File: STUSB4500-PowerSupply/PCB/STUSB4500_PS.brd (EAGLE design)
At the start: 60 x 40 mm, 90 parts, among them J2 FEMALE 2x3, J3 FEMALE 2x3, J4 FEMALE 2x3

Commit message: UART and 3V3
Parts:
- added F1: 6V/0.5A, DD_SparkFun-Fuses:1206
- added J9: (no value), DD_SparkFun-Connectors:1X03_LOCK_NO_SILK
- moved C17 1.84 mm to (17.8, 27.6), turned to 90 degrees
- moved R39 1.56 mm to (12.0, 34.6)
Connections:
- new net UART_RX: J9.2, U$8.11
- new net UART_TX: J9.1, U$8.12
- net +3V3: now also F1.2
- net GND: now also J9.3
- net VIN_2: now also F1.1
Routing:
- net +3V3: track 149.1 -> 94.3 mm, vias 8 -> 12
- net VIN_2: track 28.2 -> 82.5 mm, vias 0 -> 6
- net UART_RX: track 0.00 -> 7.32 mm
- net UART_TX: track 0.00 -> 6.15 mm
- net N$27: track 4.42 -> 2.86 mm
- net USB_D+: track 22.3 -> 21.2 mm
- net USB_D-: track 23.3 -> 22.2 mm
- net GND: vias 165 -> 167
- added copper zone on layer 16, net VIN_2
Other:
- board text added: "Dyringer"

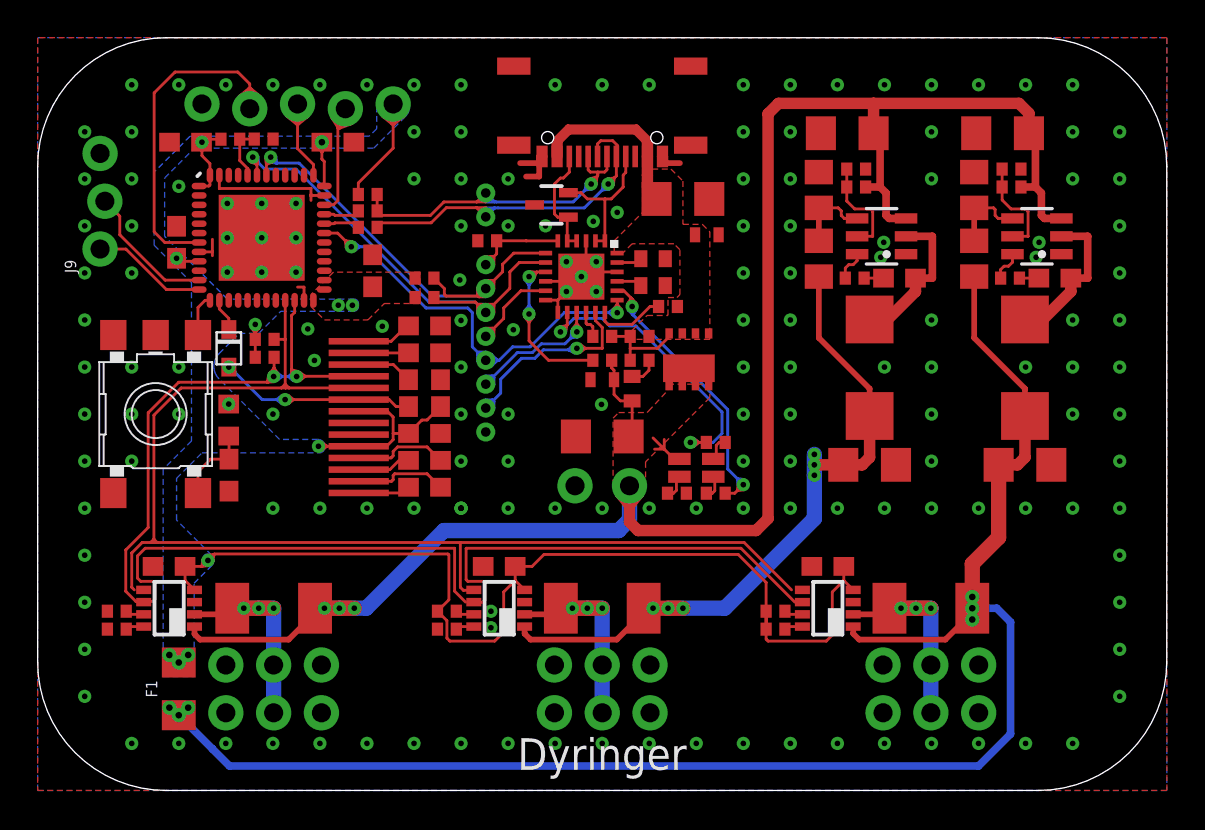
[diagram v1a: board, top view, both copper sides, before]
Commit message: Added output caps and diodes
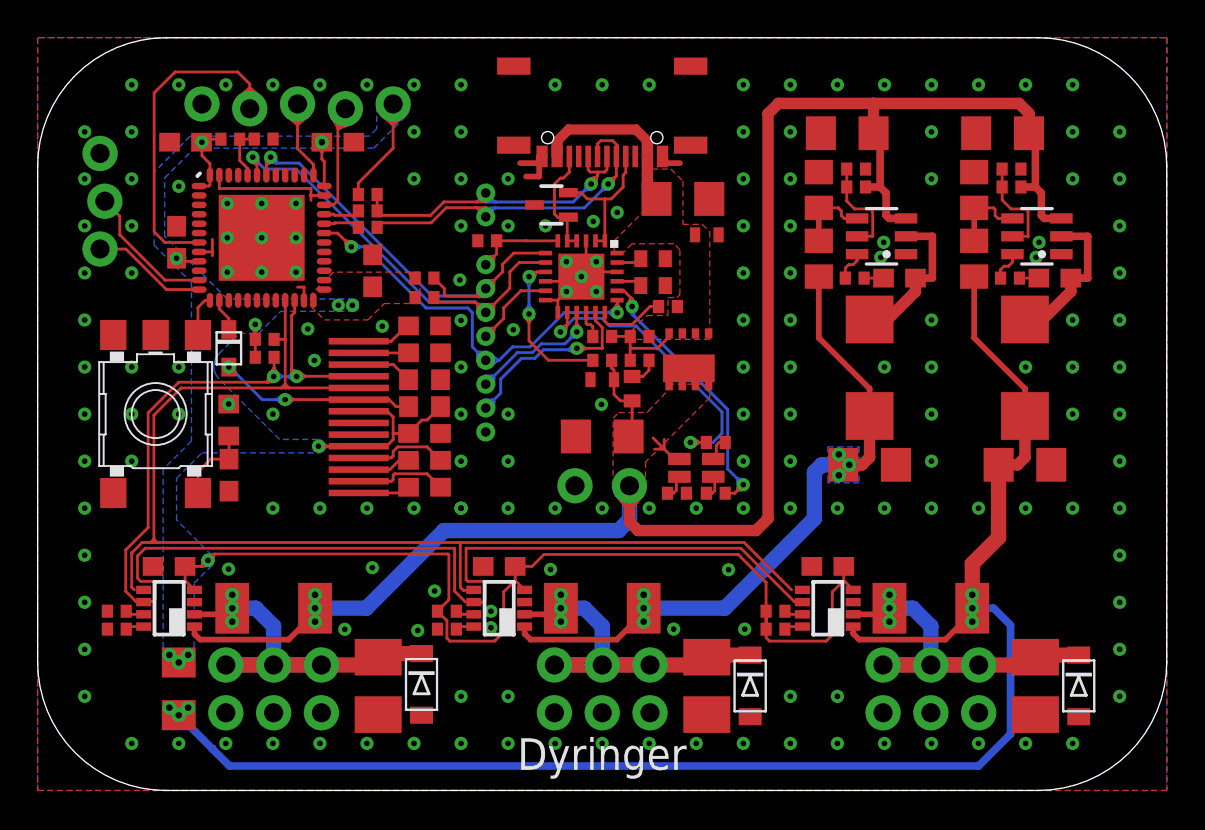
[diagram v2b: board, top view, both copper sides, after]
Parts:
- added C25, C26, C27: (no value), DD_rcl:B/3528-21R
- added D1, D3, D4: (no value), DD_adafruit:SOD-123FL
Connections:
- net VIN_1 renamed 5V0_IN
- removed net VOUT_0: J4.3, J4.4, R19.1, U$10.2
- removed net VOUT_1: J2.3, J2.4, R8.1, U$7.2
- removed net VOUT_2: J3.3, J3.4, R14.1, U$9.2
- new net 3V3_IN: C13.2, L2.2, R14.2, R24.2, U$9.1
- new net 3V3_OUT: C26.+, D3.C, J3.2, J3.4, J3.6, R14.1, U$9.2
- new net 5V0_OUT: C25.+, D4.C, J2.2, J2.4, J2.6, R8.1, U$7.2
- new net USB-PD_OUT: C27.+, D1.C, J4.2, J4.4, J4.6, R19.1, U$10.2
- net GND: now also C25.-, C26.-, C27.-, D1.A, D3.A, D4.A, J2.3, J3.3, J4.3; no longer J2.2, J2.6, J3.2, J3.6, J4.2, J4.6
- net VIN_2: no longer C13.2, L2.2, R14.2, R24.2, U$9.1
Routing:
- net VIN_2: track 82.5 -> 54.2 mm
- net 3V3_IN: track 0.00 -> 27.9 mm
- net USB-PD_OUT: track 0.00 -> 22.9 mm, vias 0 -> 3
- net 5V0_OUT: track 0.00 -> 22.3 mm, vias 0 -> 3
- net 3V3_OUT: track 0.00 -> 22.3 mm, vias 0 -> 3
- net VOUT_0: track 11.5 -> 0.00 mm, vias 3 -> 0
- net VOUT_2: track 11.4 -> 0.00 mm, vias 3 -> 0
- net VOUT_1: track 11.4 -> 0.00 mm, vias 3 -> 0
- net USB_PD_VDD: track 101.3 -> 100.2 mm
- net 5V0_IN: track 36.7 -> 35.7 mm
- net GND: vias 167 -> 180
- added copper zone on layer 16, net 3V3_OUT
- added copper zone on layer 16, net 5V0_IN
- added copper zone on layer 16, net 5V0_OUT
- added copper zone on layer 16, net USB-PD_OUT
- added copper zone on layer 16, net USB_PD_VDD

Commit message: Cleanups replaced button with adafruit one
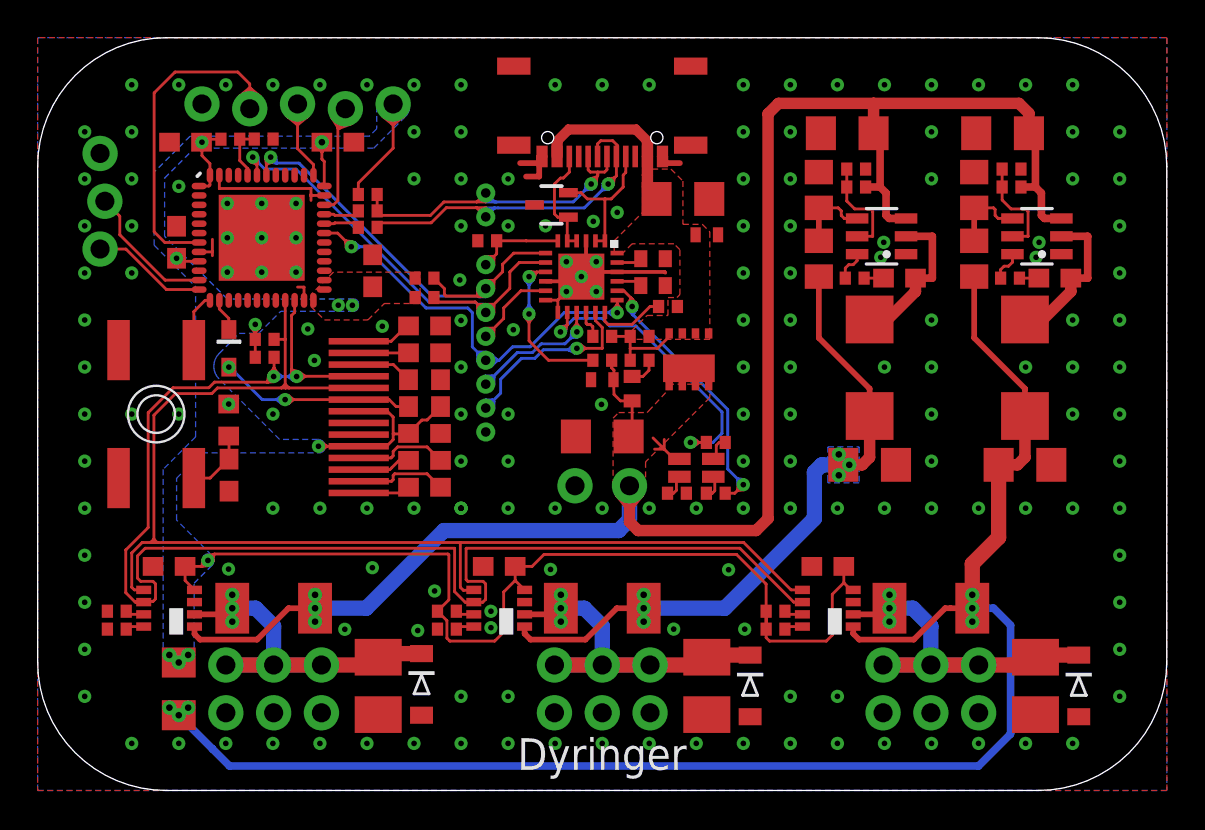
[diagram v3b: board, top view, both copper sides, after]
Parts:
- removed S1: SKHMPSE010, switch:SKHMPXE010
- added SW1: SPST_TACT-EVQQ2, DD_adafruit:EVQ-Q2
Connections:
- net GND: now also SW1.A, SW1.A'; no longer S1.1, S1.2, S1.5
- net KEY: now also SW1.B, SW1.B'; no longer S1.3, S1.4
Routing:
- net GND: track 25.2 -> 33.1 mm, vias 180 -> 177
- net SDA_2: track 82.8 -> 84.3 mm
- net SCL_2: track 66.2 -> 67.4 mm
- net USB_PD_VDD: track 100.2 -> 101.3 mm

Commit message: Updated stusb part
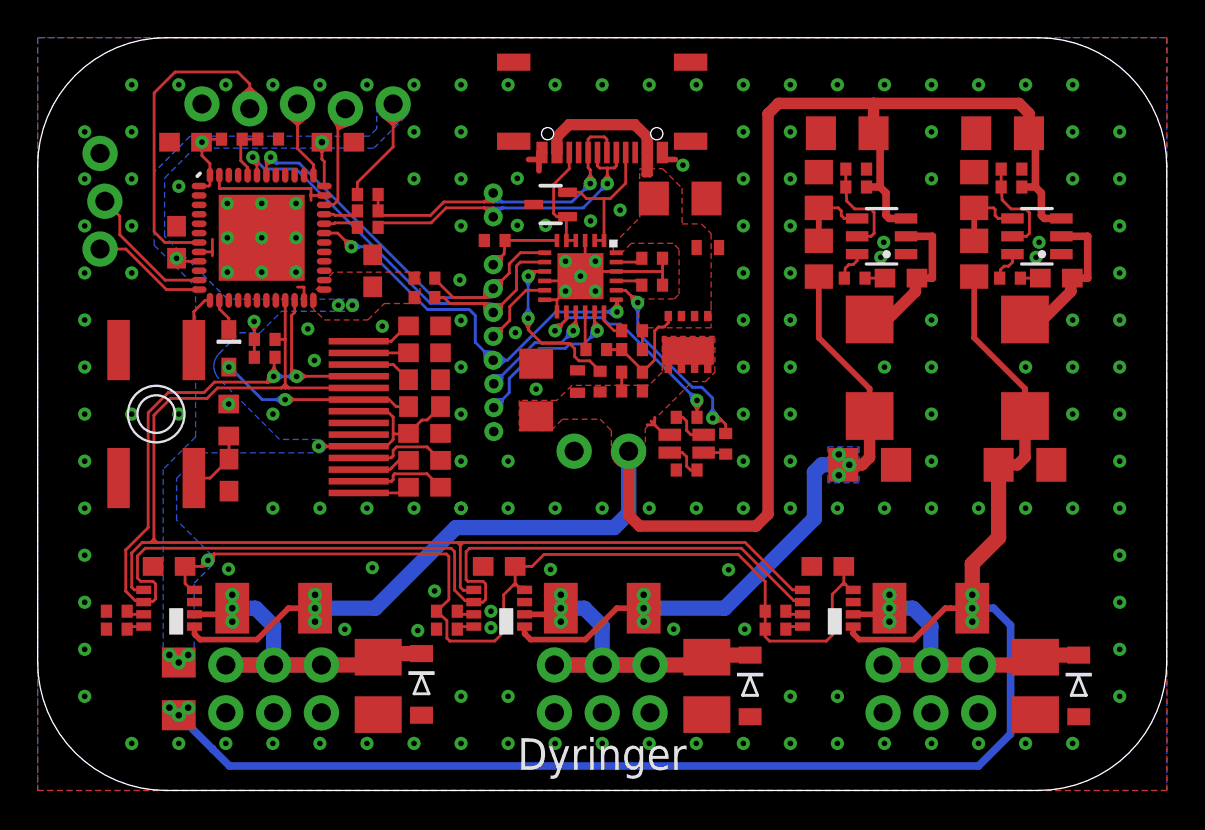
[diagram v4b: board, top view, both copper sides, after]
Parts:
- removed C1, C2: 1u, DD_rcl:C0402
- removed C3: 100n, DD_rcl:C0402
- removed C4: 4.7u, DD_rcl:C1206
- removed C5: 1u, DD_rcl:C1206
- removed ESDA25W: ESDA25WSOT323, DD_STUSB4500:SOT323
- removed J5: (no value), DD_SparkFun-Connectors:1X03_1.27MM
- removed J6: (no value), DD_SparkFun-Connectors:1X02_1.27MM
- removed J7: (no value), DD_SparkFun-Connectors:1X02_LOCK
- removed J8: (no value), DD_SparkFun-Connectors:1X05_1.27MM
- removed LED1: GM1WA55311A, led:GM1WA55311A
- removed R1, R10, R7: 1k, DD_rcl:R0402
- removed R2, R3, R36, R5: 22k, DD_rcl:R0402
- removed R4: 100k, DD_rcl:R0402
- removed R6: 100, DD_rcl:R0402
- removed U$1: STUSB4500QFN24_4X4, DD_STUSB4500:QFN24-4X4
- removed U$2: USB-C, DD_usb_c:USB-C_16P
- removed U$4, U$5: ESDA25P35, DD_STUSB4500:1610
- removed U$6: STL6P3LLH6, DD_STUSB4500:POWER_FLAT_3X3
- added C28, C29: 1u, DD_rcl:C0402
- added C30: 100n, DD_rcl:C0402
- added C31: 4.7u, DD_rcl:C1206
- added C32: 1u, DD_rcl:C1206
- added ESDA25W1: ESDA25WSOT323, DD_STUSB4500:SOT323
- added J10: (no value), DD_SparkFun-Connectors:1X02_LOCK
- added J11: (no value), DD_SparkFun-Connectors:1X05_1.27MM
- added J12: (no value), DD_SparkFun-Connectors:1X02_1.27MM
- added J13: (no value), DD_SparkFun-Connectors:1X03_1.27MM
- added LED2: GM1WA55311A, led:GM1WA55311A
- added R32, R44, R45: 1k, DD_rcl:R0402
- added R41: 100k, DD_rcl:R0402
- added R42, R46, R47, R48: 22k, DD_rcl:R0402
- added R43: 100, DD_rcl:R0402
- added U$13: USB-C, DD_usb_c:USB-C_16P
- added U$14, U$15: ESDA25P35, DD_STUSB4500:1610
- added U$16: STL6P3LLH6, DD_STUSB4500:POWER_FLAT_3X3
- added U$3: STUSB4500QFN24_4X4, DD_STUSB4500:QFN24-4X4
- moved R39 0.24 mm to (12.2, 34.6)
- moved C12 0.08 mm to (54.1, 27.2)
- moved C9 0.08 mm to (45.9, 27.2)
- moved R40 0.08 mm to (10.3, 34.6)
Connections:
- removed net N$10: ESDA25W.3, U$1.1, U$1.2, U$2.A5
- removed net N$11: ESDA25W.2, U$1.4, U$1.5, U$2.B5
- removed net N$12: R5.1, U$1.16
- removed net N$14: R10.2, U$1.9
- removed net N$16: C1.1, U$1.23
- removed net N$17: C2.1, U$1.21
- removed net N$2: LED1.1, R2.2
- removed net N$20: LED1.3, R36.2
- removed net N$3: R4.1, R5.2, R6.2, U$6.P$4
- removed net N$5: R7.2, U$1.18
- removed net N$6: LED1.2, R3.2
- removed net N$7: C3.1, R6.1
- new net N$21: R41.1, R42.2, R43.2, U$16.P$4
- new net N$31: R44.2, U$3.18
- new net N$32: ESDA25W1.3, U$13.A5, U$3.1, U$3.2
- new net N$33: ESDA25W1.2, U$13.B5, U$3.4, U$3.5
- new net N$34: R42.1, U$3.16
- new net N$42: C30.1, R43.1
- new net N$43: R45.2, U$3.9
- new net N$44: C28.1, U$3.23
- new net N$45: C29.1, U$3.21
- new net N$46: LED2.1, R46.2
- new net N$47: LED2.2, R47.2
- new net N$48: LED2.3, R48.2
- net GND: now also C28.2, C29.2, C31.2, C32.2, ESDA25W1.1, J10.2, J13.3, R32.1, R46.1, U$13.A1, U$13.A12, U$13.B1, U$13.B12, U$13.P$1, U$13.P$2, U$13.P$3, U$13.P$4, U$14.P$1, U$15.P$1, U$3.10, U$3.12, U$3.13, U$3.22, U$3.3, U$3.EXP; no longer C1.2, C2.2, C4.2, C5.2, ESDA25W.1, J5.3, J7.2, R1.1, R2.1, U$1.10, U$1.12, U$1.13, U$1.22, U$1.3, U$1.EXP, U$2.A1, U$2.A12, U$2.B1, U$2.B12, U$2.P$1, U$2.P$2, U$2.P$3, U$2.P$4, U$4.P$1, U$5.P$1
- net SCL: now also J11.2, U$3.7; no longer J8.2, U$1.7
- net SDA: now also J11.3, U$3.8; no longer J8.3, U$1.8
- net STUSB_AB: now also J13.2, U$3.17; no longer J5.2, U$1.17
- net STUSB_ALERT: now also J11.5, U$3.19; no longer J8.5, U$1.19
- net STUSB_ATTACH: now also J11.4, U$3.11; no longer J8.4, U$1.11
- net STUSB_GPIO: now also J13.1, U$3.15; no longer J5.1, U$1.15
- net STUSB_PDO2: now also R47.1, U$3.20; no longer R3.1, U$1.20
- net STUSB_PDO3: now also R48.1, U$3.14; no longer R36.1, U$1.14
- net STUSB_RST: now also J11.1, R32.2, U$3.6; no longer J8.1, R1.2, U$1.6
- net USB_D+: now also J12.1, U$13.A6, U$13.B6; no longer J6.1, U$2.A6, U$2.B6
- net USB_D-: now also J12.2, U$13.A7, U$13.B7; no longer J6.2, U$2.A7, U$2.B7
- net USB_PD_VDD: now also C30.2, C32.1, J10.1, LED2.4, R45.1, U$15.P$2, U$16.P$5, U$16.P$6, U$16.P$7, U$16.P$8, U$16.P$9; no longer C3.2, C5.1, J7.1, LED1.4, R10.1, U$5.P$2, U$6.P$5, U$6.P$6, U$6.P$7, U$6.P$8, U$6.P$9
- net VDD: now also C31.1, R41.2, R44.1, U$13.A4, U$13.A9, U$13.B4, U$13.B9, U$14.P$2, U$16.P$1, U$16.P$2, U$16.P$3, U$3.24; no longer C4.1, R4.2, R7.1, U$1.24, U$2.A4, U$2.A9, U$2.B4, U$2.B9, U$4.P$2, U$6.P$1, U$6.P$2, U$6.P$3
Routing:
- net N$43: track 0.00 -> 14.1 mm, vias 0 -> 2
- net N$14: track 13.3 -> 0.00 mm, vias 2 -> 0
- net N$32: track 0.00 -> 7.92 mm
- net N$10: track 7.72 -> 0.00 mm
- net USB_PD_VDD: track 101.3 -> 94.3 mm
- net N$33: track 0.00 -> 6.24 mm
- net N$21: track 0.00 -> 6.18 mm
- net N$11: track 6.12 -> 0.00 mm
- net GND: track 33.1 -> 27.8 mm, vias 177 -> 179
- net N$3: track 4.75 -> 0.00 mm
- net STUSB_PDO3: track 21.0 -> 17.2 mm
- net N$5: track 3.79 -> 0.00 mm
- net STUSB_PDO2: track 19.5 -> 16.2 mm
- net N$48: track 0.00 -> 2.13 mm
- net N$46: track 0.00 -> 2.13 mm
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
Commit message: Cleanups in BOM, fixed OLED layout
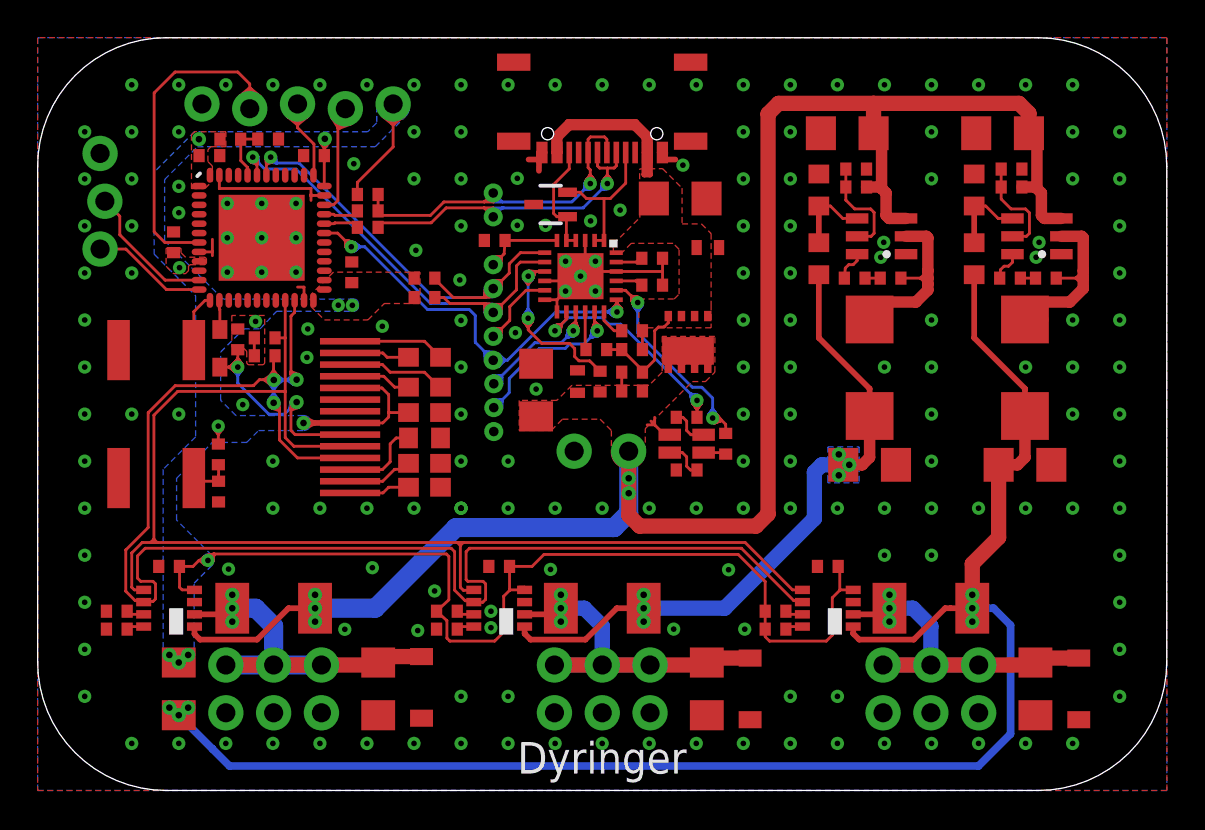
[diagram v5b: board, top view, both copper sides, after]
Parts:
- C10, C13: value (none) -> 22uF 6.3V
- C11, C14: value (none) -> 10uF 25V
- C12, C6, C7, C8, C9: value (none) -> 100nF 25V; device DD_rcl:C0603 -> DD_rcl:C0402
- C15, C16, C17, C18, C19: value 100n -> 100nF 25V; device DD_rcl:C0603 -> DD_rcl:C0402
- C20, C21: value (none) -> 10uF 6.3V
- C22, C23, C24: value (none) -> 1uF 25V
- C25, C26: value (none) -> 22uF 6.3V; device DD_rcl:B/3528-21R -> DD_rcl:C1206
- C27: value (none) -> 10uF 25V; device DD_rcl:B/3528-21R -> DD_rcl:C1206
- C28, C29: value 1u -> 1uF 6.3V
- C30: value 100n -> 100nF 25V
- C31: value 4.7u -> 10uF 25V
- C32: value 1u -> 10uF 25V
- L1: value (none) -> 5.6uH
- L2: value (none) -> 4.7uH
- R11, R23: value (none) -> 30
- R12: value (none) -> 52.3k; device DD_rcl:R0805 -> DD_rcl:R0603
- R14, R19, R8: value 10m -> 0.1R
- R15, R25: value (none) -> 10k; device DD_rcl:R0805 -> DD_rcl:R0603
- R24: value (none) -> 31.6k; device DD_rcl:R0805 -> DD_rcl:R0603
- R31: value 10K -> 10k; device DD_rcl:R0603 -> DD_rcl:R0402
- R35: device DD_rcl:R0603 -> DD_rcl:R0402
- moved R31 10.5 mm to (10.6, 24.0), turned to 90 degrees
- moved C20 8.57 mm to (20.6, 16.1)
- moved C24 6.91 mm to (20.6, 23.0), turned to 0 degrees
- moved C21 5.87 mm to (20.6, 17.4)
- moved C23 3.89 mm to (20.6, 21.4), turned to 0 degrees
- moved R30 3.10 mm to (20.6, 18.7)
- moved R35 1.91 mm to (9.60, 17.9)
- moved C16 1.46 mm to (14.7, 33.7), turned to 180 degrees
- moved C15 1.46 mm to (9.13, 33.7), turned to 0 degrees
- moved C17 1.11 mm to (16.7, 27.5)
- moved C22 1.11 mm to (20.6, 20.1)
- moved C18 1.03 mm to (9.61, 15.9)
- moved C12 0.56 mm to (53.6, 27.2)
- moved C9 0.56 mm to (45.3, 27.2)
- moved D2 0.48 mm to (9.68, 23.5)
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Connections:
- net 3V3_OUT: now also C26.1; no longer C26.+
- net 5V0_OUT: now also C25.1; no longer C25.+
- net GND: now also C25.2, C26.2, C27.2; no longer C25.-, C26.-, C27.-
- net USB-PD_OUT: now also C27.1; no longer C27.+
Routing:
- net STUSB_PDO2: track 16.2 -> 44.0 mm
- net STUSB_PDO3: track 17.2 -> 39.5 mm
- net STUSB_ALERT: track 28.5 -> 47.6 mm
- net N$43: track 14.1 -> 30.4 mm
- net STUSB_GPIO: track 10.7 -> 25.1 mm
- net USB-PD_OUT: track 22.9 -> 37.0 mm
- net 5V0_OUT: track 22.7 -> 36.8 mm
- net 3V3_OUT: track 22.7 -> 36.8 mm
- net STUSB_AB: track 12.8 -> 24.7 mm
- net USB_D+: track 22.1 -> 33.4 mm
- net GND: track 27.8 -> 37.8 mm, vias 179 -> 186
- net 5V0_IN: track 35.8 -> 45.5 mm
- net USB_PD_VDD: track 94.3 -> 103.4 mm, vias 3 -> 5
- net SDA_2: track 83.9 -> 92.8 mm, vias 2 -> 3
- net OLED_RST: track 14.2 -> 22.4 mm
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
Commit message: Cleanups
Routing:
- net SDA: track 36.0 -> 34.7 mm
- net N$43: track 30.4 -> 29.4 mm
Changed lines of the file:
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@@
 <wire x1="11.748196875" y1="33.3368" x2="11.39620625" y2="33.38006875" width="0.1524" layer="16"/>
 <wire x1="11.39620625" y1="33.38006875" x2="11.396203125" y2="33.38006875" width="0.1524" layer="16"/>
-<wire x1="11.65625" y1="33.2660125" x2="11.70443125" y2="33.617365625" width="0.1524" layer="16"/>
-<wire x1="11.43" y1="33.655" x2="11.70443125" y2="33.617365625" width="0.1524" layer="16"/>
-<wire x1="11.65625" y1="33.2660125" x2="11.327021875" y2="33.39785" width="0.1524" layer="16"/>
-<wire x1="11.43" y1="33.655" x2="11.327021875" y2="33.39785" width="0.1524" layer="16"/>
 <wire x1="11.748196875" y1="33.336803125" x2="11.704928125" y2="33.68879375" width="0.1524" layer="16"/>
 <wire x1="11.43" y1="33.655" x2="11.704928125" y2="33.68879375" width="0.1524" layer="16"/>
@@
 <wire x1="26.04248125" y1="25.543128125" x2="26.275309375" y2="25.275615625" width="0.1524" layer="16"/>
 <wire x1="26.06636875" y1="25.0937625" x2="26.275309375" y2="25.275615625" width="0.1524" layer="16"/>
-<wire x1="26.06636875" y1="26.87814375" x2="26.286203125" y2="27.156428125" width="0.1524" layer="1"/>
 <wire x1="26.06884375" y1="27.3281375" x2="26.286203125" y2="27.156428125" width="0.1524" layer="1"/>
-<wire x1="26.06636875" y1="26.87814375" x2="25.84960625" y2="27.15883125" width="0.1524" layer="1"/>
-<wire x1="26.06884375" y1="27.3281375" x2="25.84960625" y2="27.15883125" width="0.1524" layer="1"/>
 <wire x1="26.06636875" y1="26.87814375" x2="26.286203125" y2="27.156428125" width="0.1524" layer="16"/>
 <wire x1="26.06884375" y1="27.3281375" x2="26.286203125" y2="27.156428125" width="0.1524" layer="16"/>

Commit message: Added alternate 3V3 source
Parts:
- added C1: 10uF 6.3V, DD_rcl:C0603
- added D5: 1N4148, DD_adafruit:SOD-323F
- added U$1: TLV704_3V3SOT23-5, DD_TLV704:SOT23-5
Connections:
- removed net VIN_2: F1.1
- new net N$2: C1.2, D5.A, U$1.3
- net +3V3: now also D5.C
- net 3V3_IN: now also F1.1
- net GND: now also C1.1, U$1.1, U$1.4, U$1.5
- net UART_RX: now also J9.1; no longer J9.2
- net UART_TX: now also J9.2, U$8.10; no longer J9.1, U$8.12
- net VDD: now also U$1.2
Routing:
- net VIN_2: track 61.9 -> 0.00 mm, vias 6 -> 0
- net 3V3_IN: track 28.1 -> 90.0 mm, vias 0 -> 5
- net VDD: track 19.1 -> 27.6 mm
- net N$2: track 0.00 -> 4.47 mm
- net UART_TX: track 6.15 -> 7.51 mm
- net UART_RX: track 7.32 -> 6.19 mm
- added copper zone on layer 16, net 3V3_IN
- removed copper zone on layer 16, net VIN_2
